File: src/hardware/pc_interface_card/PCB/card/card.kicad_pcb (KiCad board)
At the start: 2 copper layers, 91.6 x 100 mm, 63 parts, among them J1 USBC_IO_PWR, J2 USBC_PWR_ONLY, J3 10018784-10201TLF, J4 PD_I2C, Q1 STL6P3LLH6, Q2 STL6P3LLH6, U1 NCP1117-5.0, U2 FT230XQ, U3 THVD1450DR, U4 STUSB4500QTR, U5 STUSB4500QTR

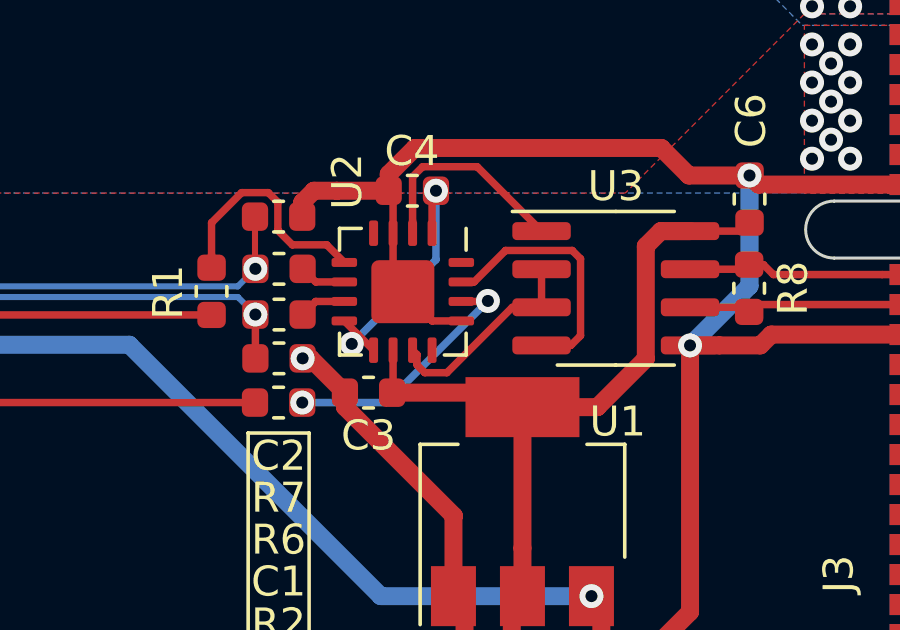
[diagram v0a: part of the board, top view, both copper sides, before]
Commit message: Changing ~RE connection in U3 THVD1450DR to GND to always enable receiving from the RS485 bus to better handle error and collision detections Fixing symbol library location
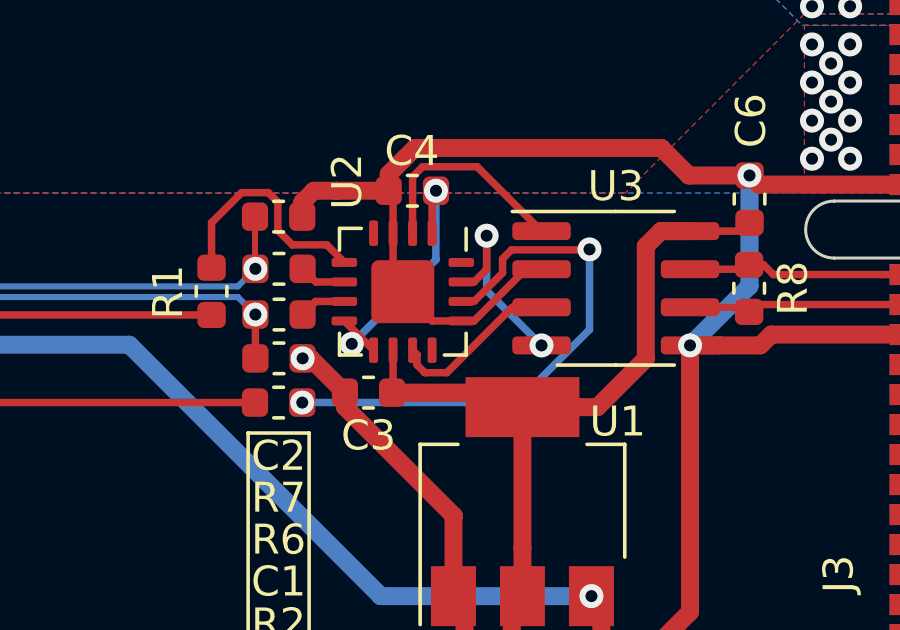
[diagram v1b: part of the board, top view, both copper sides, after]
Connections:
- U3 pad 2: /RS485/FT_TXDEN -> GND
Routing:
- net /FT_RXLED: track 8.48 -> 18.5 mm
- net GND: track 208.4 -> 211.8 mm
- net /RS485/FT_TXD: track 8.52 -> 6.56 mm, vias 0 -> 2
- net /RS485/FT_TXDEN: track 6.98 -> 5.71 mm

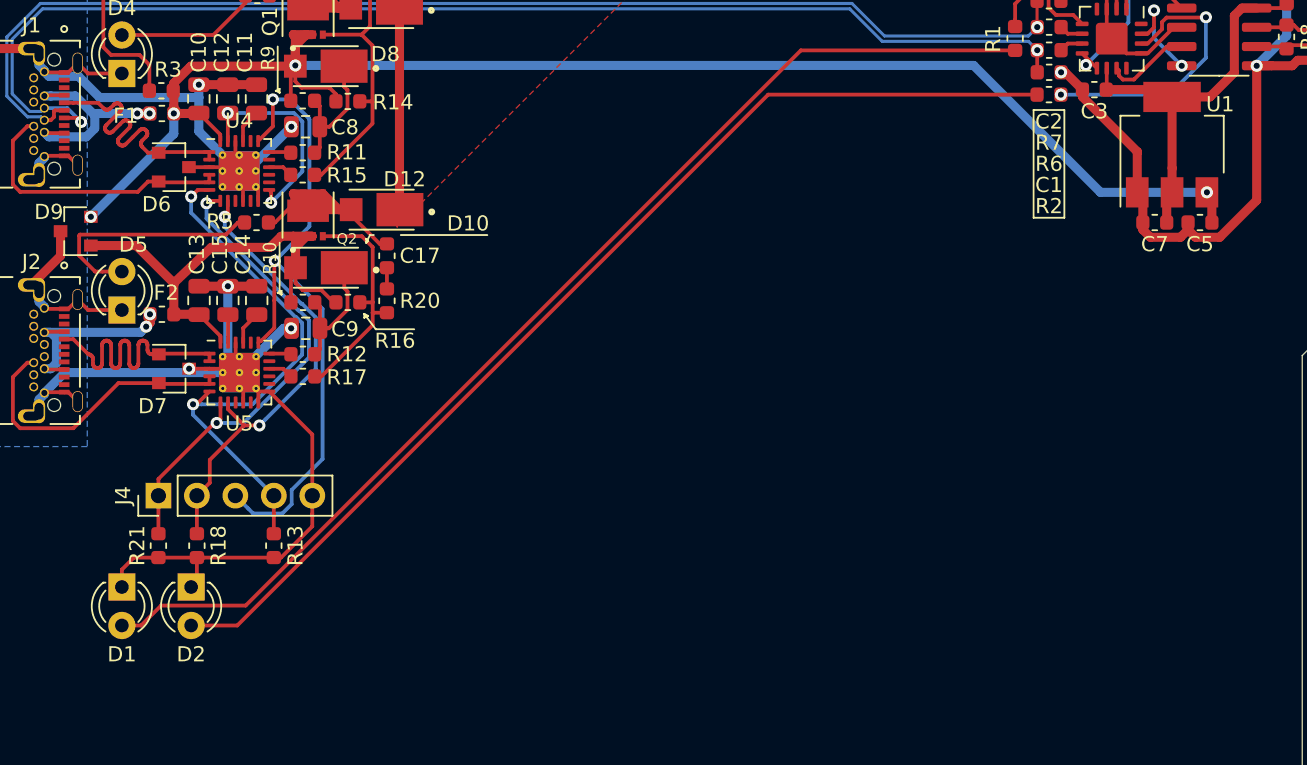
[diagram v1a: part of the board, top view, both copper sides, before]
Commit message: Fixing RXLED and TXLED polarization
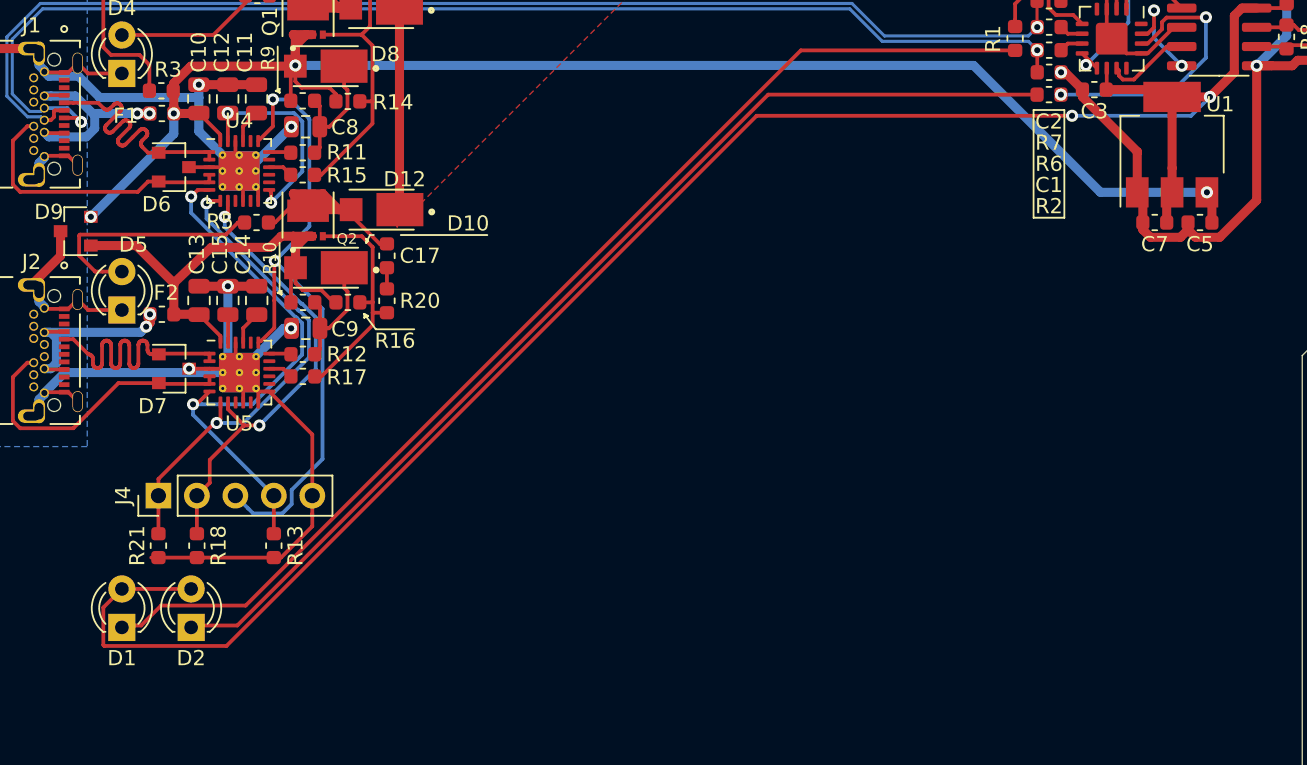
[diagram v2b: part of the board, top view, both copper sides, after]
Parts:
- moved D1 2.67 mm to (112.8, 124.0), turned to 90 degrees
- moved D2 2.67 mm to (117.3, 124.0), turned to 90 degrees
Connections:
- C3 pad 1: /RS485/PB_5V -> /FT_PB_5V
- C6 pad 1: /RS485/PB_5V -> /FT_PB_5V
- C7 pad 1: /RS485/PB_5V -> /FT_PB_5V
- D1 pad 1: GND -> Net-(D1-Pad1)
- D1 pad 2: Net-(D1-Pad2) -> /FT_PB_5V
- D2 pad 1: GND -> Net-(D2-Pad1)
- D2 pad 2: Net-(D2-Pad2) -> /FT_PB_5V
- R1 pad 2: Net-(D1-Pad2) -> Net-(D1-Pad1)
- R2 pad 2: Net-(D2-Pad2) -> Net-(D2-Pad1)
- U1 pad 2: /RS485/PB_5V -> /FT_PB_5V
- U2 pad 10: /RS485/PB_5V -> /FT_PB_5V
- U3 pad 8: /RS485/PB_5V -> /FT_PB_5V
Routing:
- net /FT_PB_5V: track 0.00 -> 124.2 mm, vias 0 -> 2
- net Net-(D1-Pad1): track 0.00 -> 74.8 mm
- net Net-(D1-Pad2): track 74.7 -> 0.00 mm
- net Net-(D2-Pad1): track 0.00 -> 70.4 mm
- net Net-(D2-Pad2): track 70.4 -> 0.00 mm
- net /RS485/PB_5V: track 26.7 -> 0.00 mm
- net GND: track 211.8 -> 206.2 mm

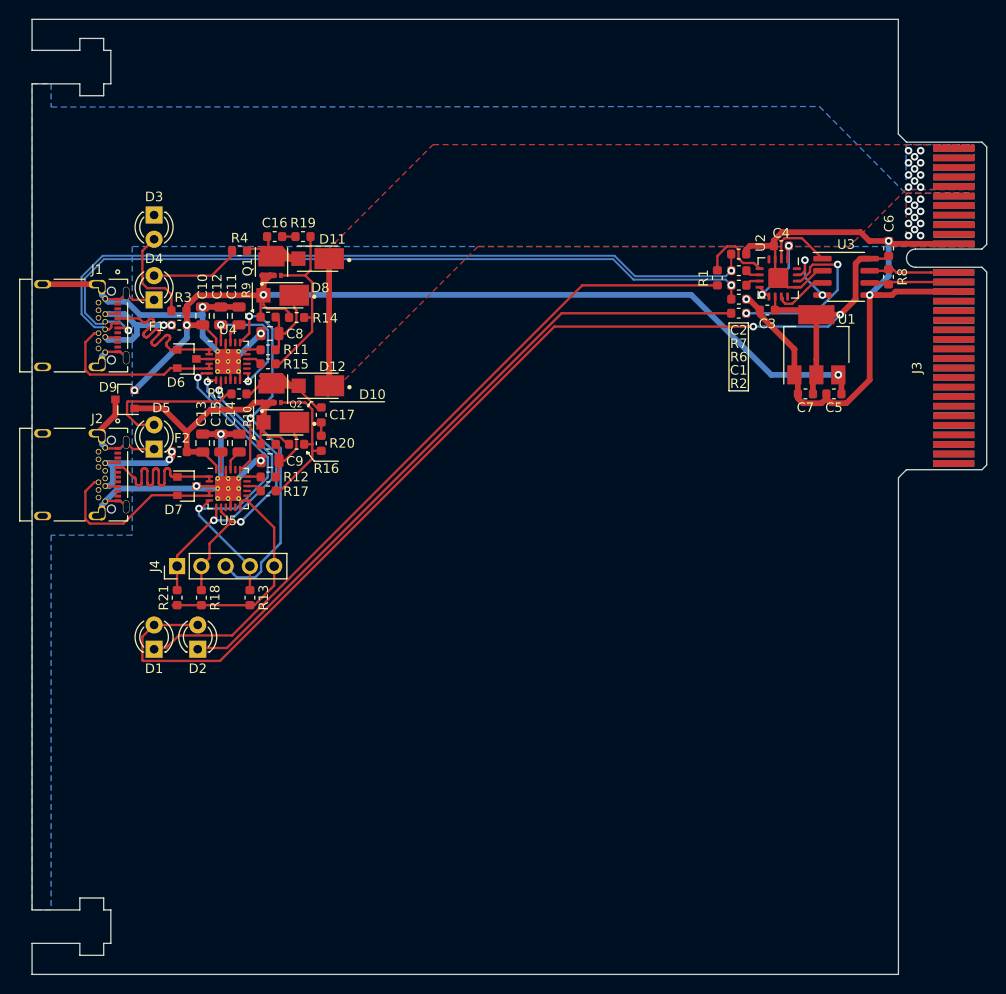
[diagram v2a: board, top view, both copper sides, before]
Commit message: adding barrel jack connector for powering PC interface card and mooving the status LEDs on the front panel
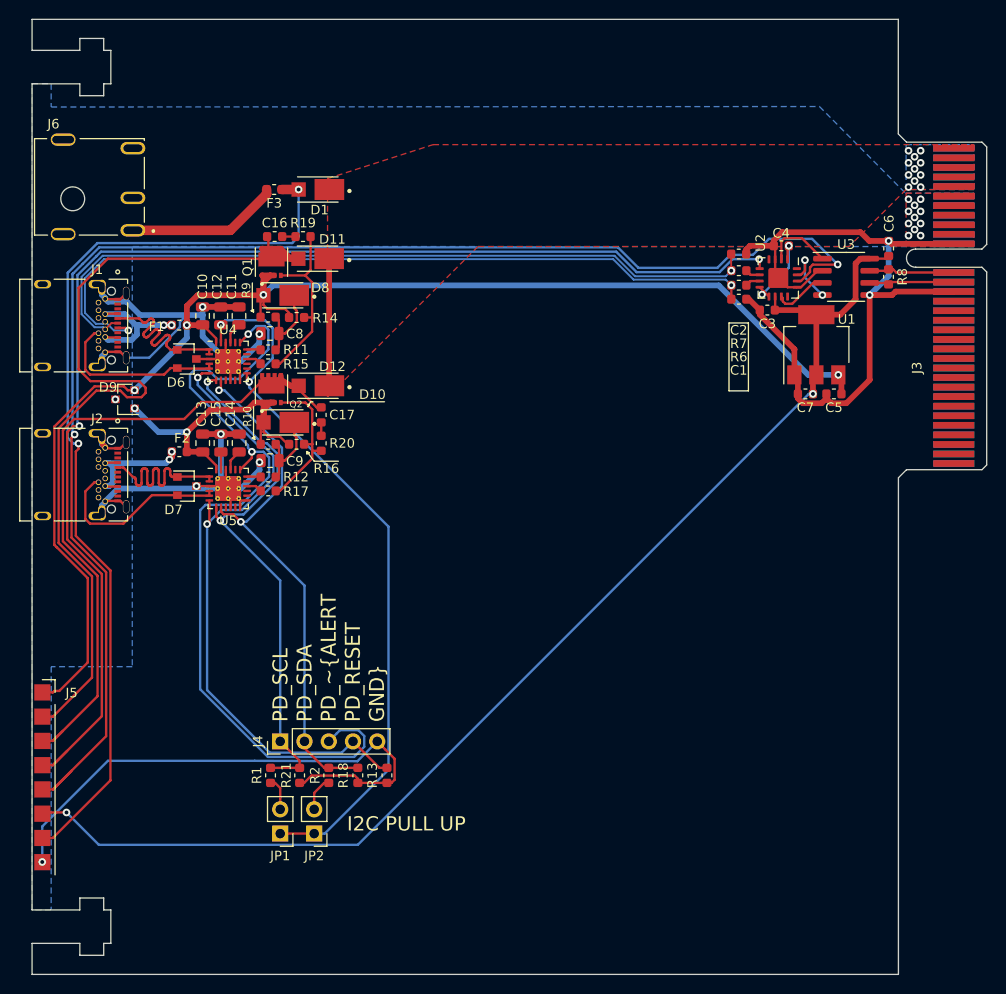
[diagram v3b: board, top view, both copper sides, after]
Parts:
- removed D2, D3, D4, D5: LED, LED_THT:LED_D3.0mm
- removed R3, R4, R5: 1k, Resistor_SMD:R_0603_1608Metric
- added F3: 3A, Fuse:Fuse_0603_1608Metric, F.Cu at (125.3, 75.8)
- added J5: EDG_CONN, Connector_PinSocket_2.54mm:PinSocket_1x08_P2.54mm_Vertical, F.Cu at (101.1, 128.5)
- added J6: BARREL_JACK_PWR_ONLY, kicad-lib:CUI_PJ-079BH, F.Cu at (100.3, 76.8)
- added JP1: I2C_PU, Connector_PinHeader_2.54mm:PinHeader_1x02_P2.54mm_Vertical, F.Cu at (126.0, 143.3)
- added JP2: I2C_PU, Connector_PinHeader_2.54mm:PinHeader_1x02_P2.54mm_Vertical, F.Cu at (129.5, 143.3)
- D1: value LED -> V4PAN50-M3; footprint LED_THT:LED_D3.0mm -> kicad-lib:SMPA
- R1, R2: value 270 -> 22k
- moved R1 70.0 mm to (125.0, 137.2), turned to 90 degrees
- moved R2 64.7 mm to (131.1, 137.2), turned to 90 degrees
- moved D1 51.1 mm to (129.9, 75.8), turned to 180 degrees
- moved R18 24.8 mm to (134.1, 137.2)
- moved R13 23.5 mm to (137.2, 137.2)
- moved R21 22.6 mm to (128.0, 137.2)
- moved J4 21.3 mm to (126.0, 133.6)
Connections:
- D1 pad 1: Net-(D1-Pad1) -> /PB_12V
- D1 pad 2: /FT_PB_5V -> /JACK_PWR_OK
- J1 pad A8: Net-(J1-PadA8) -> (no net)
- J1 pad B8: Net-(J1-PadB8) -> (no net)
- J2 pad A6: Net-(J2-PadA6) -> (no net)
- J2 pad A7: Net-(J2-PadA7) -> (no net)
- J2 pad A8: Net-(J2-PadA8) -> (no net)
- J2 pad B6: Net-(J2-PadB6) -> (no net)
- J2 pad B7: Net-(J2-PadB7) -> (no net)
- J2 pad B8: Net-(J2-PadB8) -> (no net)
- J3 pad A12: Net-(J3-PadA12) -> (no net)
- J3 pad A13: Net-(J3-PadA13) -> (no net)
- J3 pad A14: Net-(J3-PadA14) -> (no net)
- J3 pad A15: Net-(J3-PadA15) -> (no net)
- J3 pad A16: Net-(J3-PadA16) -> (no net)
- J3 pad A17: Net-(J3-PadA17) -> (no net)
- J3 pad A18: Net-(J3-PadA18) -> (no net)
- J3 pad A19: Net-(J3-PadA19) -> (no net)
- J3 pad A20: Net-(J3-PadA20) -> (no net)
- J3 pad A21: Net-(J3-PadA21) -> (no net)
- J3 pad A22: Net-(J3-PadA22) -> (no net)
- J3 pad A23: Net-(J3-PadA23) -> (no net)
- J3 pad A24: Net-(J3-PadA24) -> (no net)
- J3 pad A25: Net-(J3-PadA25) -> (no net)
- J3 pad A26: Net-(J3-PadA26) -> (no net)
- J3 pad A27: Net-(J3-PadA27) -> (no net)
- J3 pad A28: Net-(J3-PadA28) -> (no net)
- J3 pad A29: Net-(J3-PadA29) -> (no net)
- J3 pad A30: Net-(J3-PadA30) -> (no net)
- J3 pad A31: Net-(J3-PadA31) -> (no net)
- J3 pad A32: Net-(J3-PadA32) -> (no net)
- J3 pad B15: Net-(J3-PadB15) -> (no net)
- J3 pad B16: Net-(J3-PadB16) -> (no net)
- J3 pad B17: Net-(J3-PadB17) -> (no net)
- J3 pad B18: Net-(J3-PadB18) -> (no net)
- J3 pad B19: Net-(J3-PadB19) -> (no net)
- J3 pad B20: Net-(J3-PadB20) -> (no net)
- J3 pad B21: Net-(J3-PadB21) -> (no net)
- J3 pad B22: Net-(J3-PadB22) -> (no net)
- J3 pad B23: Net-(J3-PadB23) -> (no net)
- J3 pad B24: Net-(J3-PadB24) -> (no net)
- J3 pad B25: Net-(J3-PadB25) -> (no net)
- J3 pad B26: Net-(J3-PadB26) -> (no net)
- J3 pad B27: Net-(J3-PadB27) -> (no net)
- J3 pad B28: Net-(J3-PadB28) -> (no net)
- J3 pad B29: Net-(J3-PadB29) -> (no net)
- J3 pad B30: Net-(J3-PadB30) -> (no net)
- J3 pad B31: Net-(J3-PadB31) -> (no net)
- J3 pad B32: Net-(J3-PadB32) -> (no net)
- R1 pad 1: /FT_TXLED -> Net-(JP1-Pad2)
- R1 pad 2: Net-(D1-Pad1) -> /PD_SCL
- R2 pad 1: /FT_RXLED -> Net-(JP2-Pad2)
- R2 pad 2: Net-(D2-Pad1) -> /PD_SDA
- U2 pad 12: Net-(U2-Pad12) -> (no net)
- U2 pad 16: Net-(U2-Pad16) -> (no net)
- U2 pad 4: Net-(U2-Pad4) -> (no net)
- U4 pad 11: Net-(U4-Pad11) -> (no net)
- U4 pad 14: Net-(U4-Pad14) -> (no net)
- U4 pad 15: Net-(U4-Pad15) -> (no net)
- U4 pad 17: Net-(U4-Pad17) -> (no net)
- U4 pad 20: Net-(U4-Pad20) -> (no net)
- U4 pad 9: Net-(U4-Pad9) -> (no net)
- U5 pad 11: Net-(U5-Pad11) -> (no net)
- U5 pad 14: Net-(U5-Pad14) -> (no net)
- U5 pad 15: Net-(U5-Pad15) -> (no net)
- U5 pad 17: Net-(U5-Pad17) -> (no net)
- U5 pad 20: Net-(U5-Pad20) -> (no net)
- U5 pad 9: Net-(U5-Pad9) -> (no net)
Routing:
- net /FT_RXLED: track 18.5 -> 151.7 mm
- net /FT_TXLED: track 7.85 -> 134.0 mm, vias 0 -> 2
- net /JACK_PWR_OK: track 0.00 -> 97.6 mm, vias 0 -> 2
- net /USB_A_PWR_OK: track 11.4 -> 93.8 mm
- net Net-(D1-Pad1): track 74.8 -> 0.00 mm
- net Net-(D2-Pad1): track 70.4 -> 0.00 mm
- net /USB_PD/PB_2V7: track 14.1 -> 76.2 mm
- net /USB_B_PWR_OK: track 14.8 -> 71.4 mm
- net /USBC_IO_PWR_CONN_VBUS: track 102.2 -> 145.5 mm
- net /PD_~ALERT: track 45.0 -> 86.8 mm
- net /PD_RESET: track 35.6 -> 67.6 mm
- net GND: track 206.2 -> 237.4 mm, vias 19 -> 20
- net /PD_SDA: track 30.4 -> 55.9 mm
- net /PD_SCL: track 32.3 -> 56.3 mm
- net Net-(F3-Pad2): track 0.00 -> 16.1 mm
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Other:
- board text added: "I2C PULL UP"
- board text added: "PD_SCL PD_SDA PD_~ALERT PD_RESET GND"
